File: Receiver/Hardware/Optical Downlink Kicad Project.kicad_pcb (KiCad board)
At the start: 2 copper layers, 18 parts, among them J1 Conn_01x20_Socket, J2 Conn_01x20_Socket, U1 OPA657U, U2 TLE2426-EP_D_8, U3 OPA657U, U4 ADS8691IPWR, U5 MEV3S0515SC, U6 HT7580-2

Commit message: Worked on Assigning Cap and R footprints
Also fixed an issue with some missing capacitors
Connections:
- U2 pad 3: VDD -> Op Amp Voltage Source
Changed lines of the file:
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@@
 	(net 55 "unconnected-(U2-NC-Pad5)")
 	(net 56 "unconnected-(U2-NC-Pad6)")
-	(net 57 "VDD")
-	(net 58 "unconnected-(U2-NC-Pad7)")
-	(net 59 "unconnected-(U2-NC-Pad4)")
-	(net 60 "unconnected-(U3-NC-Pad8)")
-	(net 61 "unconnected-(U3-NC-Pad5)")
-	(net 62 "unconnected-(U3-NC-Pad1)")
-	(net 63 "unconnected-(U4-RVS-Pad15)")
-	(net 64 "DVDD")
-	(net 65 "unconnected-(U6-NC-Pad4)")
-	(net 66 "GND")
+	(net 57 "unconnected-(U2-NC-Pad7)")
+	(net 58 "unconnected-(U2-NC-Pad4)")
+	(net 59 "unconnected-(U3-NC-Pad8)")
+	(net 60 "unconnected-(U3-NC-Pad5)")
+	(net 61 "unconnected-(U3-NC-Pad1)")
+	(net 62 "unconnected-(U4-RVS-Pad15)")
+	(net 63 "DVDD")
+	(net 64 "unconnected-(U6-NC-Pad4)")
+	(net 65 "GND")
 	(footprint "Connector_PinHeader_2.54mm:PinHeader_1x20_P2.54mm_Vertical"
 		(layer "F.Cu")
@@
 			(size 1.454899 0.558)
 			(layers "F.Cu" "F.Mask" "F.Paste")
-			(net 62 "unconnected-(U3-NC-Pad1)")
+			(net 61 "unconnected-(U3-NC-Pad1)")
 			(pinfunction "NC")
 			(pintype "no_connect")
@@
 			(size 1.454899 0.558)
 			(layers "F.Cu" "F.Mask" "F.Paste")
-			(net 66 "GND")
+			(net 65 "GND")
 			(pinfunction "VS-")
 			(pintype "power_in")
@@
 			(size 1.454899 0.558)
 			(layers "F.Cu" "F.Mask" "F.Paste")
-			(net 61 "unconnected-(U3-NC-Pad5)")
+			(net 60 "unconnected-(U3-NC-Pad5)")
 			(pinfunction "NC")
 			(pintype "no_connect")
@@
 			(size 1.454899 0.558)
 			(layers "F.Cu" "F.Mask" "F.Paste")
-			(net 60 "unconnected-(U3-NC-Pad8)")
+			(net 59 "unconnected-(U3-NC-Pad8)")
 			(pinfunction "NC")
 			(pintype "no_connect")
@@
 			(size 2.2 1.6)
 			(layers "F.Cu" "F.Mask" "F.Paste")
-			(net 66 "GND")
+			(net 65 "GND")
 			(pintype "passive")
 		)
@@
 			(size 2.2 1.6)
 			(layers "F.Cu" "F.Mask" "F.Paste")
-			(net 66 "GND")
+			(net 65 "GND")
 			(pintype "passive")
 		)
@@
 			(size 1.4732 0.3556)
 			(layers "F.Cu" "F.Mask" "F.Paste")
-			(net 66 "GND")
+			(net 65 "GND")
 			(pinfunction "DGND")
 			(pintype "power_in")
@@
 			(size 1.4732 0.3556)
 			(layers "F.Cu" "F.Mask" "F.Paste")
-			(net 66 "GND")
+			(net 65 "GND")
 			(pinfunction "AGND")
 			(pintype "power_in")
@@
 			(size 1.4732 0.3556)
 			(layers "F.Cu" "F.Mask" "F.Paste")
-			(net 66 "GND")
+			(net 65 "GND")
 			(pinfunction "REFGND")
 			(pintype "power_in")
@@
 			(size 1.4732 0.3556)
 			(layers "F.Cu" "F.Mask" "F.Paste")
-			(net 66 "GND")
+			(net 65 "GND")
 			(pinfunction "AIN_GND")
 			(pintype "input")
@@
 			(size 1.4732 0.3556)
 			(layers "F.Cu" "F.Mask" "F.Paste")
-			(net 63 "unconnected-(U4-RVS-Pad15)")
+			(net 62 "unconnected-(U4-RVS-Pad15)")
 			(pinfunction "RVS")
 			(pintype "output+no_connect")
@@
 			(size 1.4732 0.3556)
 			(layers "F.Cu" "F.Mask" "F.Paste")
-			(net 64 "DVDD")
+			(net 63 "DVDD")
 			(pinfunction "DVDD")
 			(pintype "power_in")
@@
 			)
 		)
-		(property "Datasheet" "TLE2426-EP_D_8"
+		(property "Datasheet" "https://www.ti.com/lit/ds/symlink/tle2426.pdf?ts=1770316456619&ref_url=https%253A%252F%252Fwww.ti.com%252Fproduct%252FTLE2426%253Futm_source%253Dgoogle%2526utm_medium%253Dcpc%2526utm_campaign%253Dasc-amps-null-44700045336317116_prodfolderdynamic-cpc-pf-google-ww_en_int%2526utm_content%253Dprodfolddynamic%2526ds_k%253DDYNAMIC+SEARCH+ADS%2526DCM%253Dyes%2526gclsrc%253Daw.ds%2526gad_source%253D1%2526gad_campaignid%253D6465287935%2526gbraid%253D0AAAAAC068F23-iCzD67nAsz3YLuWpuvxn%2526gclid%253DCj0KCQiAnJHMBhDAARIsABr7b85h10I6EwIfzYnf3neIYwRcxhgcUg80GLbkkjlQ0HxPIpCeqVqFJUoaAtMjEALw_wcB"
 			(at 0 0 90)
 			(layer "F.Fab")
@@
 			(size 1.454899 0.558)
 			(layers "F.Cu" "F.Mask" "F.Paste")
-			(net 66 "GND")
+			(net 65 "GND")
 			(pinfunction "COMMON")
 			(pintype "unspecified")
@@
 			(size 1.454899 0.558)
 			(layers "F.Cu" "F.Mask" "F.Paste")
-			(net 57 "VDD")
+			(net 52 "Op Amp Voltage Source")
 			(pinfunction "IN")
 			(pintype "input")
@@
 			(size 1.454899 0.558)
 			(layers "F.Cu" "F.Mask" "F.Paste")
-			(net 59 "unconnected-(U2-NC-Pad4)")
+			(net 58 "unconnected-(U2-NC-Pad4)")
 			(pinfunction "NC")
 			(pintype "no_connect")
@@
 			(size 1.454899 0.558)
 			(layers "F.Cu" "F.Mask" "F.Paste")
-			(net 58 "unconnected-(U2-NC-Pad7)")
+			(net 57 "unconnected-(U2-NC-Pad7)")
 			(pinfunction "NC")
 			(pintype "no_connect")
@@
 			(size 2.2 1.6)
 			(layers "F.Cu" "F.Mask" "F.Paste")
-			(net 66 "GND")
+			(net 65 "GND")
 			(pintype "passive")
 		)
@@
 			(size 2.2 1.6)
 			(layers "F.Cu" "F.Mask" "F.Paste")
-			(net 66 "GND")
+			(net 65 "GND")
 			(pintype "passive")
 		)
@@
 			(layers "F.Cu" "F.Mask" "F.Paste")
 			(roundrect_rratio 0.229358)
-			(net 66 "GND")
+			(net 65 "GND")
 			(pintype "passive")
 		)
@@
 			(layers "*.Cu" "*.Mask")
 			(remove_unused_layers no)
-			(net 66 "GND")
+			(net 65 "GND")
 			(pinfunction "-VIN")
 			(pintype "power_in")
@@
 			(layers "*.Cu" "*.Mask")
 			(remove_unused_layers no)
-			(net 66 "GND")
+			(net 65 "GND")
 			(pinfunction "-VOUT")
 			(pintype "power_in")
@@
 			(layers "F.Cu" "F.Mask" "F.Paste")
 			(roundrect_rratio 0.229358)
-			(net 66 "GND")
+			(net 65 "GND")
 			(pintype "passive")
 		)
@@
 			(layers "F.Cu" "F.Mask" "F.Paste")
 			(roundrect_rratio 0.25)
-			(net 66 "GND")
+			(net 65 "GND")
 			(pinfunction "GND")
 			(pintype "input")
@@
 			(layers "F.Cu" "F.Mask" "F.Paste")
 			(roundrect_rratio 0.25)
-			(net 65 "unconnected-(U6-NC-Pad4)")
+			(net 64 "unconnected-(U6-NC-Pad4)")
 			(pinfunction "NC")
 			(pintype "no_connect")
@@
 			(size 1.454899 0.558)
 			(layers "F.Cu" "F.Mask" "F.Paste")
-			(net 66 "GND")
+			(net 65 "GND")
 			(pinfunction "VS-")
 			(pintype "power_in")
@@
 			(size 2.2 1.6)
 			(layers "F.Cu" "F.Mask" "F.Paste")
-			(net 66 "GND")
+			(net 65 "GND")
 			(pintype "passive")
 		)

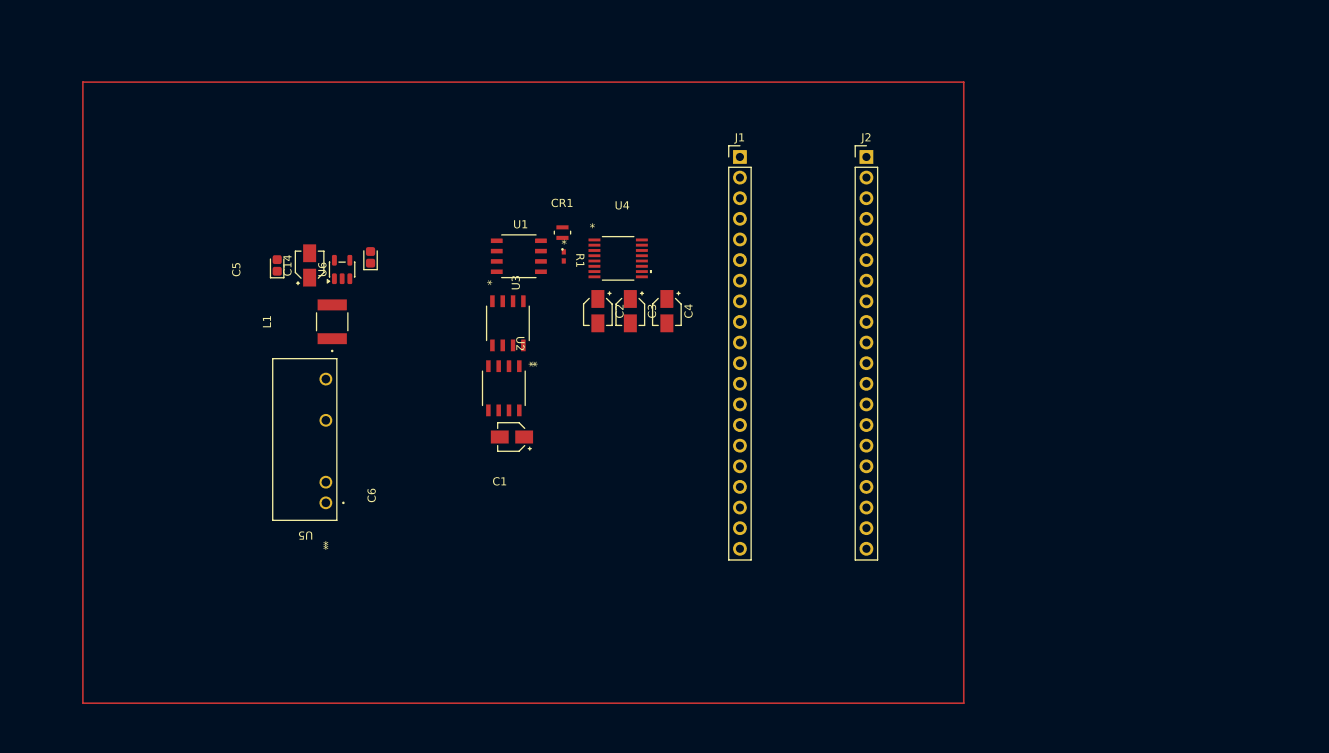
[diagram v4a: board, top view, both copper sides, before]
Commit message: Finished General Layout of PCB
Everything is pretty much finished for traces except gnd connections and clearing drc errors.
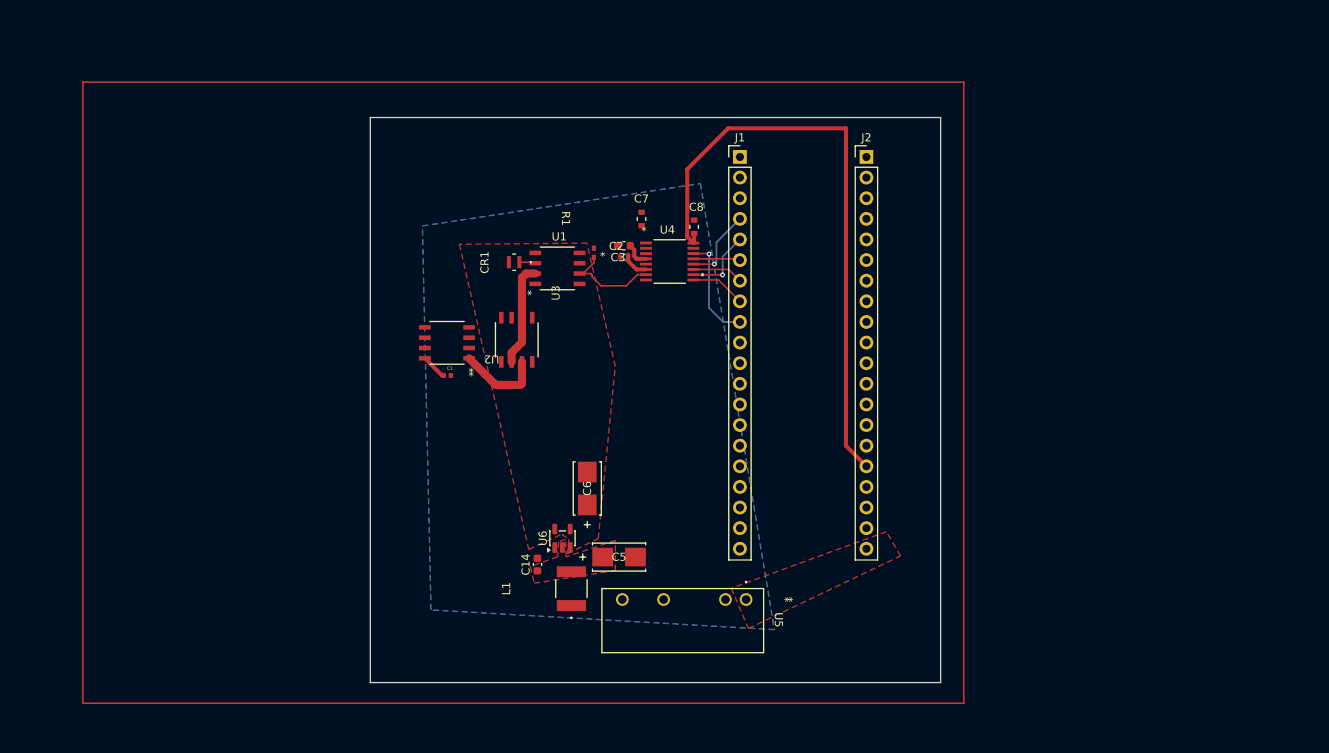
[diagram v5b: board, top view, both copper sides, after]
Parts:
- removed C4: 1u, Capacitor_SMD:CP_Elec_3x5.3
- added C7: 1u, 00-footprint-library:CAP_CL10_SAM, F.Cu at (116.3, 64.4)
- added C8: 1u, 00-footprint-library:CAP_CL10_SAM, F.Cu at (122.8, 65.3)
- C1: footprint Capacitor_SMD:CP_Elec_3x5.3 -> 00-footprint-library:CAPC1005X55N
- C14, C2: footprint Capacitor_SMD:CP_Elec_3x5.3 -> Capacitor_SMD:C_0603_1608Metric
- C3: footprint Capacitor_SMD:CP_Elec_3x5.3 -> Capacitor_SMD:C_0402_1005Metric
- C5, C6: footprint Capacitor_Tantalum_SMD:CP_EIA-1608-08_AVX-J -> 00-footprint-library:CAPMP6.3X3.2_2.8N_KEM
- U5: value MEV3S0515SC -> MEVS0509SC
- moved C5 55.4 mm to (113.5, 106.0), turned to 0 degrees
- moved U5 53.1 mm to (129.2, 111.2), turned to -90 degrees
- moved C14 46.3 mm to (103.5, 106.9)
- moved L1 44.1 mm to (107.7, 109.9)
- moved U6 42.8 mm to (106.6, 103.7)
- moved C6 39.0 mm to (109.6, 97.6)
- moved C1 11.0 mm to (92.4, 83.6), turned to 0 degrees
- moved U2 8.96 mm to (92.3, 79.6), turned to 180 degrees
- moved C2 8.67 mm to (114.2, 67.7), turned to 180 degrees
- moved CR1 6.98 mm to (100.6, 69.7), turned to 180 degrees
- moved C3 6.70 mm to (114.2, 69.0), turned to 180 degrees
- moved U4 6.36 mm to (119.8, 69.6)
- moved U1 4.98 mm to (105.9, 70.4)
- moved R1 3.73 mm to (110.4, 68.5)
- moved U3 2.31 mm to (100.9, 79.2)
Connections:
- U4 pad 16: DVDD -> 3V3
- U4 pad 2: 3V3 -> VBUS
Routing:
- net 3V3: track 0.00 -> 74.9 mm
- net ALARM: track 0.00 -> 13.1 mm, vias 0 -> 1
- net Virtual Ground: track 0.00 -> 12.8 mm
- net Signal: track 0.00 -> 12.5 mm
- net Net-(U2-OUT): track 0.00 -> 10.6 mm
- net SPI_SCK: track 0.00 -> 9.46 mm, vias 0 -> 1
- net SPI_SDI: track 0.00 -> 8.86 mm, vias 0 -> 1
- net RESET: track 0.00 -> 6.82 mm
- net SPI_CS: track 0.00 -> 6.30 mm
- net SPI_SDO: track 0.00 -> 5.79 mm
- net Net-(U4-REFCAP): track 0.00 -> 3.42 mm
- net Net-(U2-NOISEREDUCTION): track 0.00 -> 3.21 mm
- net Net-(U4-REFIO): track 0.00 -> 3.09 mm
- net Net-(U1--): track 0.00 -> 2.01 mm
- added copper zone on B.Cu, net GND
- added copper zone on F.Cu, net Intermeditate Power
- added copper zone on F.Cu, net Op Amp Voltage Source
- added copper zone on F.Cu, net VBUS
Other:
- board outline added: 70.2 x 69.6 mm
- board text added: "Connect Things to GND Net"
- board text removed: "ADC circuit"
- board text removed: "Virtual Ground and Tranimpedance amp"
- board text removed: "boost converter and LDO"

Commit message: Fixed Issues with DRC ready to be checked
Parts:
- moved C1 1.66 mm to (90.8, 83.2)
- moved CR1 0.36 mm to (100.7, 69.3)
- moved C2 0.34 mm to (113.8, 67.7)
- moved C3 0.28 mm to (113.9, 69.0)
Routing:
- net GND: track 0.00 -> 22.3 mm, vias 0 -> 16
- net Op Amp Voltage Source: track 0.00 -> 10.6 mm
- net Net-(U1--): track 2.01 -> 10.9 mm
- net Net-(U5-+VOUT): track 0.00 -> 6.59 mm
- net Intermeditate Power: track 0.00 -> 3.91 mm
- net Virtual Ground: track 12.8 -> 15.7 mm
- net VBUS: track 0.00 -> 2.62 mm
- net Net-(U2-NOISEREDUCTION): track 3.21 -> 1.96 mm
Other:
- board text removed: "Connect Things to GND Net"

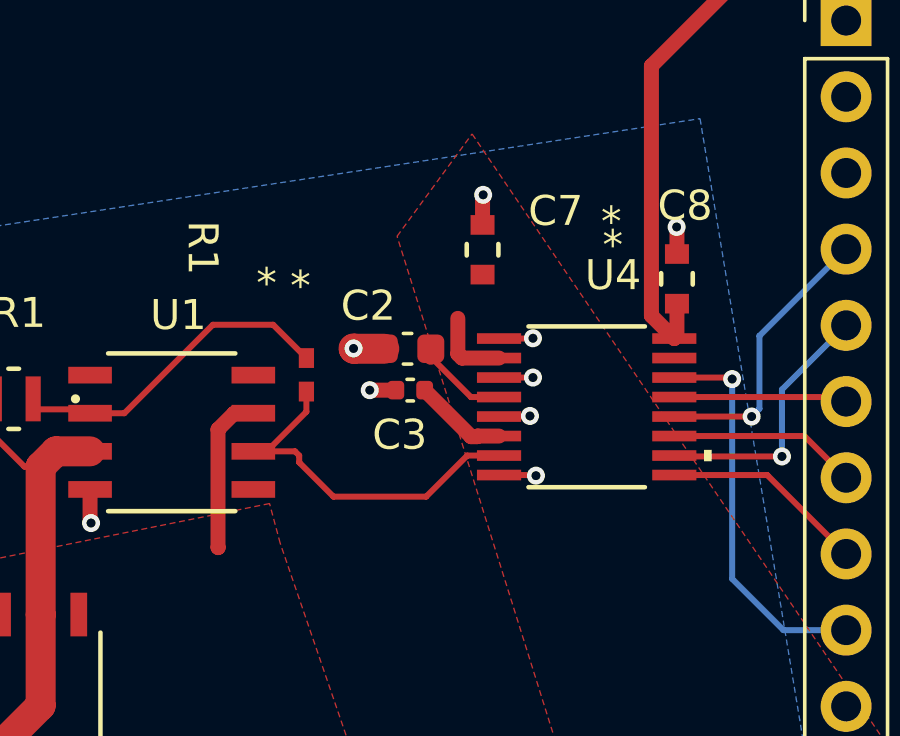
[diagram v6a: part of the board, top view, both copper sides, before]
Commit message: Cleaned Up Some of The Power Net Names
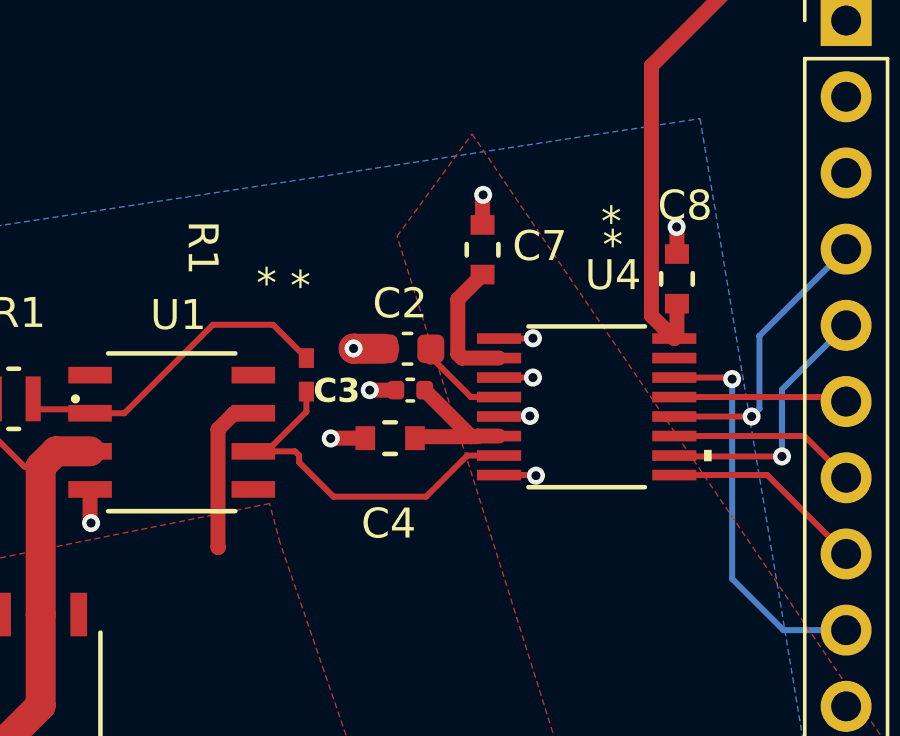
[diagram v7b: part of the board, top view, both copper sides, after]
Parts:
- added C4: 1u, 00-footprint-library:CAP_CL10_SAM, F.Cu at (113.2, 70.6)
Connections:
- net Intermeditate Power renamed +9V
- net Op Amp Voltage Source renamed +8V
- net Virtual Ground renamed +4V
- C7 pad 1: VBUS -> Net-(U4-AVDD)
- U4 pad 2: VBUS -> Net-(U4-AVDD)
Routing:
- net Net-(U4-AVDD): track 0.00 -> 4.42 mm
- net VBUS: track 2.62 -> 0.00 mm
- net Net-(U4-REFCAP): track 3.13 -> 5.02 mm
- net GND: track 22.3 -> 23.4 mm, vias 16 -> 17
